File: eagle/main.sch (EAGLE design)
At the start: 16 parts, among them IC1 74HC164D, IC2 74LS139D, Q1 BSS84, Q2 BSS84, Q3 BSS84

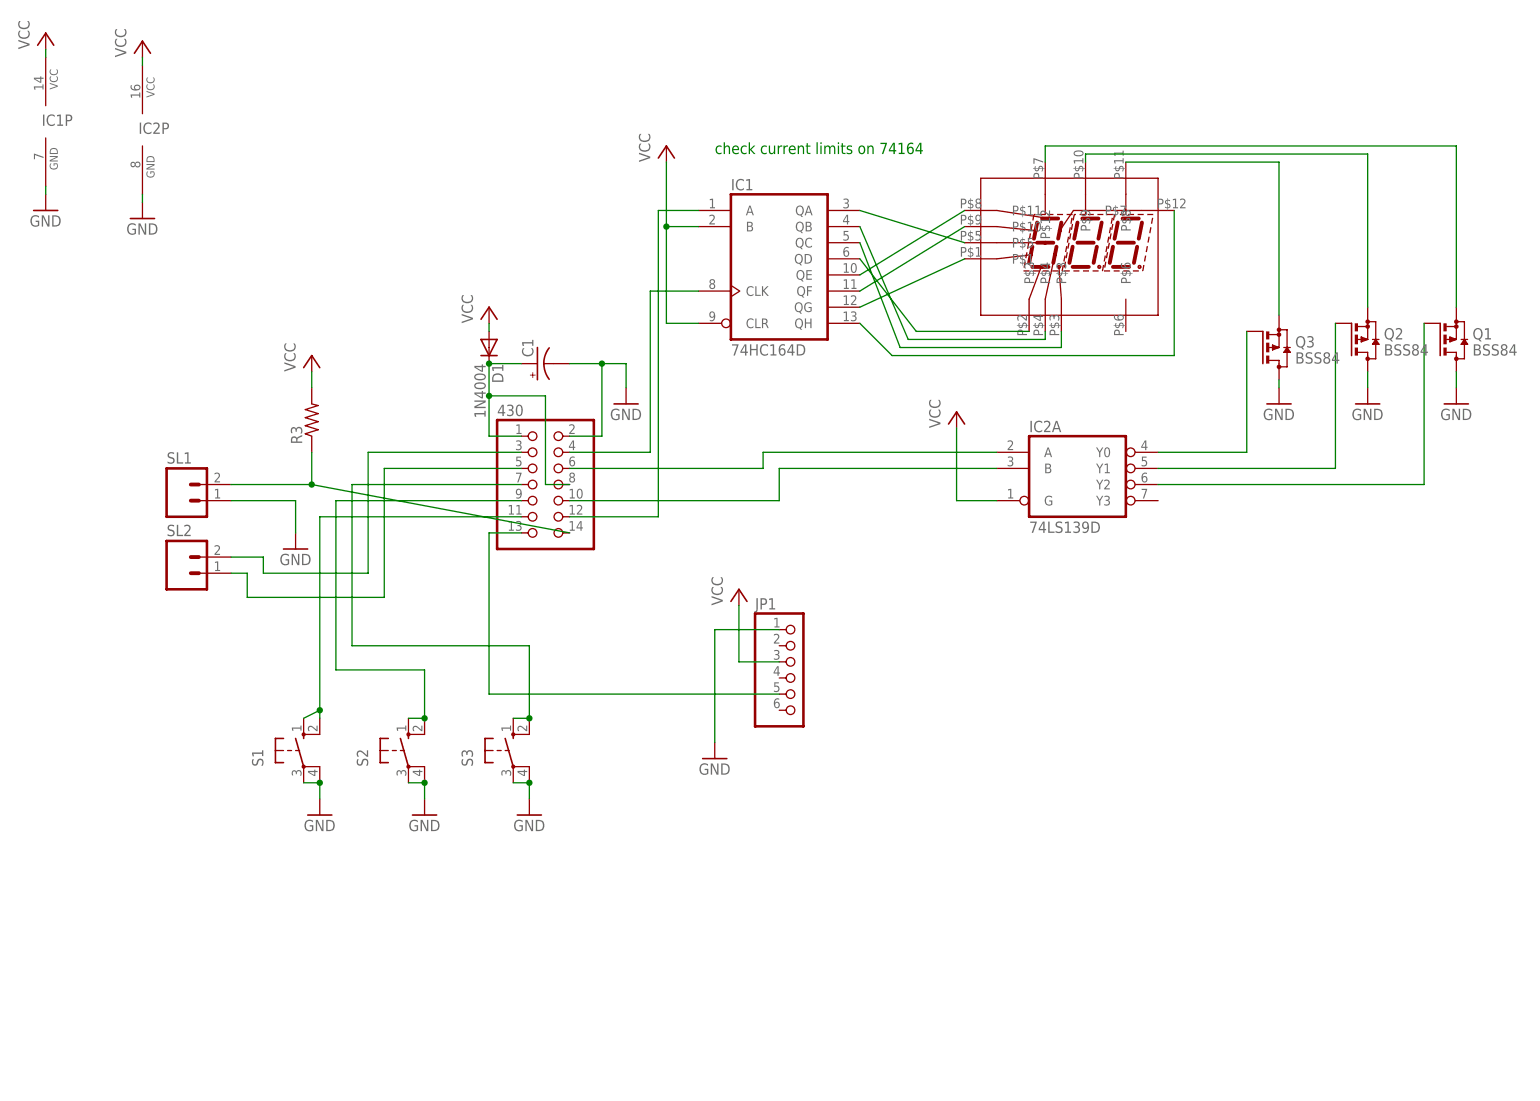
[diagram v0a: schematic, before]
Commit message: The 430 might not blow up after these edits
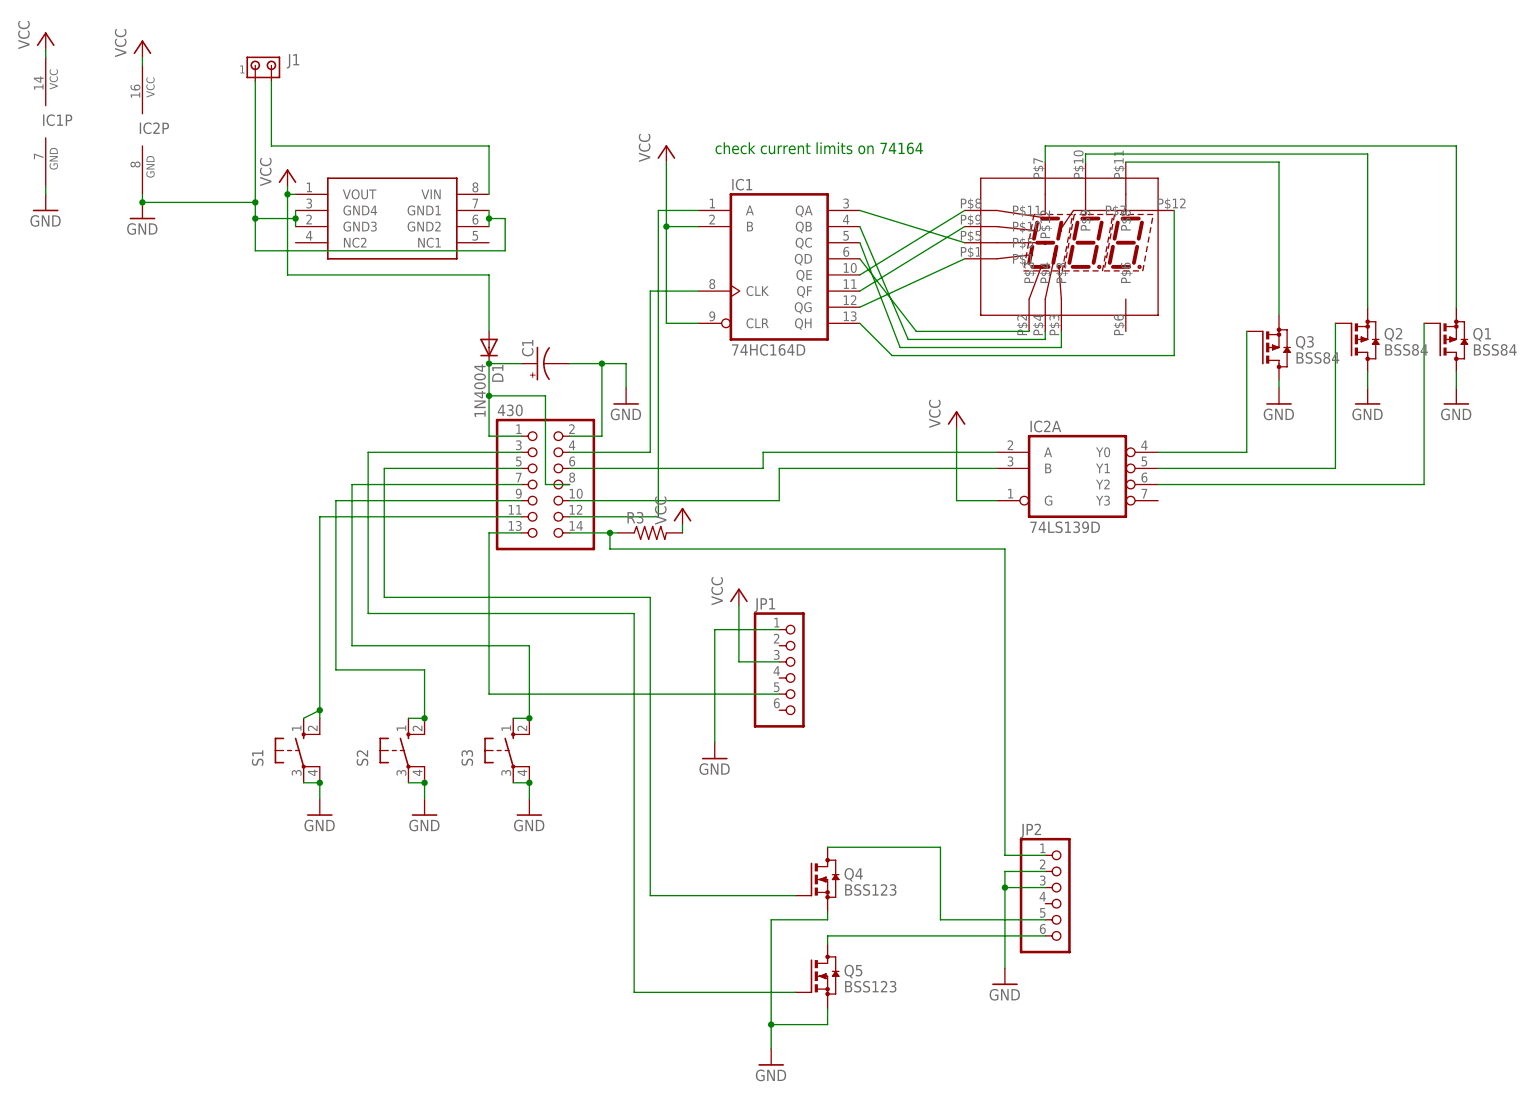
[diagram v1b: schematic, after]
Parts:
- removed SL1, SL2: (no value), con-amp-quick:M02
- added J1: (no value), con-amp:MTA02-100
- added JP2: (no value), pinhead:PINHD-1X6
- added Q4, Q5: BSS123, transistor-small-signal:BSS123
- added U$2: L78L33ABD, mjg:L78L33ABD
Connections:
- new net N$23: JP2.5, Q4.D
- new net N$28: JP2.6, Q5.D
- new net N$30: J1.2, U$2.VIN
- net GND: now also J1.1, JP2.2, JP2.3, Q4.S, Q5.S, U$2.GND1, U$2.GND2, U$2.GND3, U$2.GND4; no longer SL1.1
- net N$17: now also JP2.1; no longer SL1.2
- net N$19: now also Q5.G; no longer SL2.2
- net N$20: now also Q4.G; no longer SL2.1
- net VCC: now also U$2.VOUT
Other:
- moved on the sheet: R3

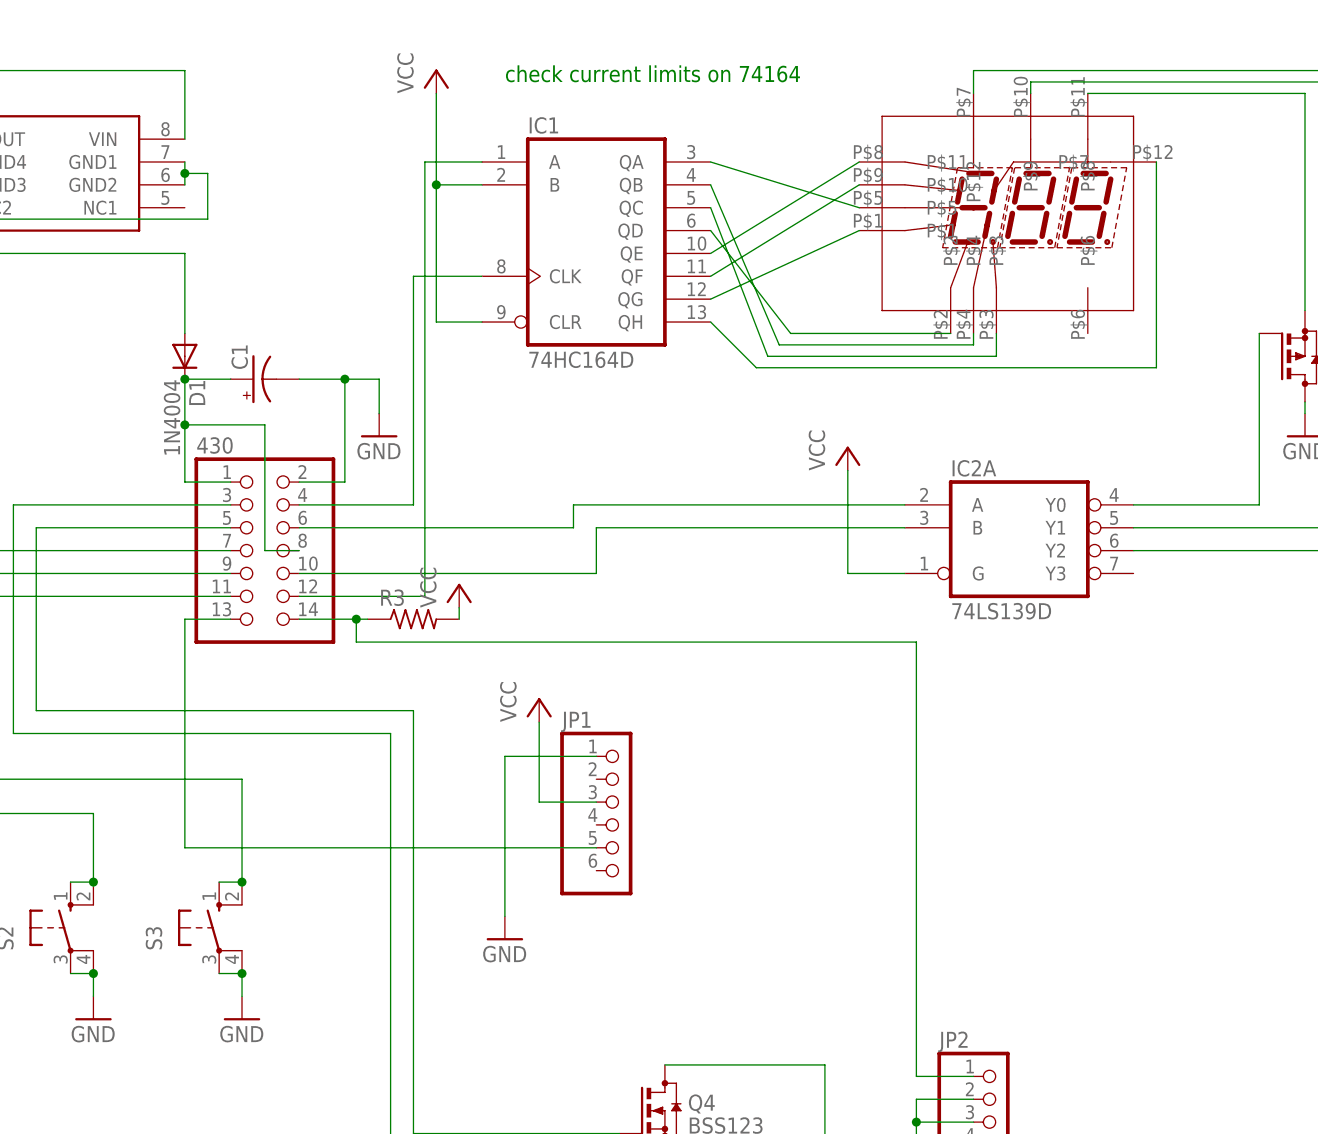
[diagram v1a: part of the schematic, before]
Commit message: updated values and added example parts order for Newark
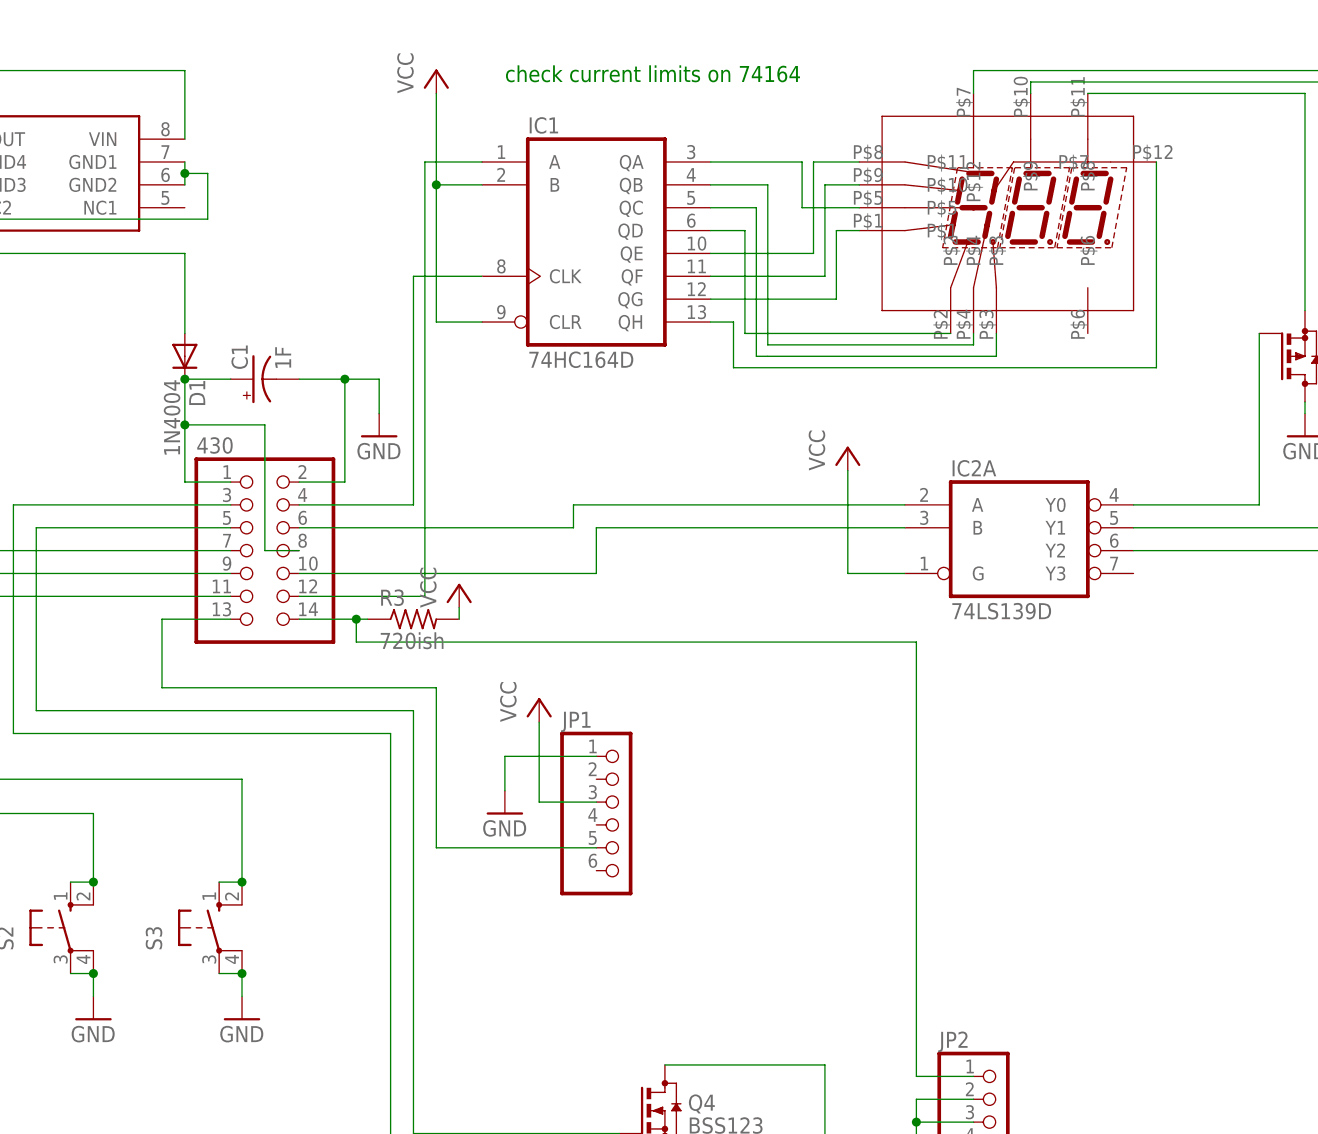
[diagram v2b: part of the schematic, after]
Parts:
- C1: value (none) -> 1F
- R3: value (none) -> 720ish
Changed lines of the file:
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@@
 <part name="P+1" library="supply1" deviceset="VCC" device=""/>
 <part name="GND1" library="supply1" deviceset="GND" device=""/>
-<part name="C1" library="rcl" deviceset="CPOL-US" device="E5-13"/>
+<part name="C1" library="rcl" deviceset="CPOL-US" device="E5-13" value="1F"/>
 <part name="D1" library="diode" deviceset="1N4004" device=""/>
-<part name="R3" library="rcl" deviceset="R-US_" device="R0805"/>
+<part name="R3" library="rcl" deviceset="R-US_" device="R0805" value="720ish"/>
 <part name="GND2" library="supply1" deviceset="GND" device=""/>
 <part name="P+3" library="supply1" deviceset="VCC" device=""/>
@@
 <instance part="IC2" gate="A" x="158.75" y="53.34"/>
 <instance part="P+5" gate="VCC" x="105.41" y="34.29"/>
-<instance part="GND7" gate="1" x="101.6" y="7.62"/>
+<instance part="GND7" gate="1" x="101.6" y="21.59"/>
 <instance part="P+6" gate="VCC" x="139.7" y="62.23"/>
 <instance part="IC1" gate="P" x="-3.81" y="107.95"/>
@@
 <segment>
 <pinref part="U$1" gate="G$1" pin="P$2"/>
-<wire x1="133.35" y1="74.93" x2="151.13" y2="74.93" width="0.1524" layer="91"/>
+<wire x1="128.27" y1="74.93" x2="151.13" y2="74.93" width="0.1524" layer="91"/>
 <pinref part="IC1" gate="A" pin="QD"/>
-<wire x1="124.46" y1="86.36" x2="133.35" y2="74.93" width="0.1524" layer="91"/>
+<wire x1="124.46" y1="86.36" x2="128.27" y2="86.36" width="0.1524" layer="91"/>
+<wire x1="128.27" y1="86.36" x2="128.27" y2="74.93" width="0.1524" layer="91"/>
 </segment>
 </net>
 <net name="N$6" class="0">
 <segment>
-<wire x1="132.08" y1="73.66" x2="153.67" y2="73.66" width="0.1524" layer="91"/>
+<wire x1="130.81" y1="73.66" x2="153.67" y2="73.66" width="0.1524" layer="91"/>
 <pinref part="U$1" gate="G$1" pin="P$4"/>
 <wire x1="153.67" y1="73.66" x2="153.67" y2="74.93" width="0.1524" layer="91"/>
 <pinref part="IC1" gate="A" pin="QB"/>
-<wire x1="124.46" y1="91.44" x2="132.08" y2="73.66" width="0.1524" layer="91"/>
+<wire x1="124.46" y1="91.44" x2="130.81" y2="91.44" width="0.1524" layer="91"/>
+<wire x1="130.81" y1="91.44" x2="130.81" y2="73.66" width="0.1524" layer="91"/>
 </segment>
 </net>
@@
 <wire x1="156.21" y1="72.39" x2="156.21" y2="74.93" width="0.1524" layer="91"/>
 <pinref part="IC1" gate="A" pin="QC"/>
-<wire x1="124.46" y1="88.9" x2="130.81" y2="72.39" width="0.1524" layer="91"/>
+<wire x1="124.46" y1="88.9" x2="129.54" y2="88.9" width="0.1524" layer="91"/>
+<wire x1="129.54" y1="88.9" x2="129.54" y2="72.39" width="0.1524" layer="91"/>
+<wire x1="129.54" y1="72.39" x2="130.81" y2="72.39" width="0.1524" layer="91"/>
 </segment>
 </net>
@@
 <segment>
 <pinref part="IC1" gate="A" pin="QH"/>
-<wire x1="124.46" y1="76.2" x2="129.54" y2="71.12" width="0.1524" layer="91"/>
-<wire x1="129.54" y1="71.12" x2="173.99" y2="71.12" width="0.1524" layer="91"/>
+<wire x1="124.46" y1="76.2" x2="127" y2="76.2" width="0.1524" layer="91"/>
+<wire x1="127" y1="76.2" x2="127" y2="71.12" width="0.1524" layer="91"/>
+<wire x1="127" y1="71.12" x2="173.99" y2="71.12" width="0.1524" layer="91"/>
 <pinref part="U$1" gate="G$1" pin="P$7"/>
 <wire x1="173.99" y1="71.12" x2="173.99" y2="93.98" width="0.1524" layer="91"/>
@@
 <pinref part="GND7" gate="1" pin="GND"/>
 <wire x1="111.76" y1="27.94" x2="101.6" y2="27.94" width="0.1524" layer="91"/>
-<wire x1="101.6" y1="27.94" x2="101.6" y2="10.16" width="0.1524" layer="91"/>
+<wire x1="101.6" y1="27.94" x2="101.6" y2="24.13" width="0.1524" layer="91"/>
 </segment>
 <segment>
@@
 <segment>
 <pinref part="430" gate="A" pin="13"/>
-<wire x1="71.12" y1="43.18" x2="66.04" y2="43.18" width="0.1524" layer="91"/>
-<wire x1="66.04" y1="43.18" x2="66.04" y2="17.78" width="0.1524" layer="91"/>
+<wire x1="71.12" y1="43.18" x2="63.5" y2="43.18" width="0.1524" layer="91"/>
+<wire x1="63.5" y1="43.18" x2="63.5" y2="35.56" width="0.1524" layer="91"/>
+<wire x1="63.5" y1="35.56" x2="93.98" y2="35.56" width="0.1524" layer="91"/>
 <pinref part="JP1" gate="A" pin="5"/>
-<wire x1="66.04" y1="17.78" x2="111.76" y2="17.78" width="0.1524" layer="91"/>
+<wire x1="93.98" y1="35.56" x2="93.98" y2="17.78" width="0.1524" layer="91"/>
+<wire x1="93.98" y1="17.78" x2="111.76" y2="17.78" width="0.1524" layer="91"/>
 </segment>
 </net>
@@
 <pinref part="IC1" gate="A" pin="QF"/>
 <pinref part="U$1" gate="G$1" pin="P$10"/>
-<wire x1="124.46" y1="81.28" x2="140.97" y2="91.44" width="0.1524" layer="91"/>
+<wire x1="124.46" y1="81.28" x2="137.16" y2="81.28" width="0.1524" layer="91"/>
+<wire x1="137.16" y1="81.28" x2="137.16" y2="91.44" width="0.1524" layer="91"/>
+<wire x1="137.16" y1="91.44" x2="140.97" y2="91.44" width="0.1524" layer="91"/>
 </segment>
 </net>
@@
 <pinref part="IC1" gate="A" pin="QE"/>
 <pinref part="U$1" gate="G$1" pin="P$11"/>
-<wire x1="124.46" y1="83.82" x2="140.97" y2="93.98" width="0.1524" layer="91"/>
+<wire x1="124.46" y1="83.82" x2="135.89" y2="83.82" width="0.1524" layer="91"/>
+<wire x1="135.89" y1="83.82" x2="135.89" y2="93.98" width="0.1524" layer="91"/>
+<wire x1="135.89" y1="93.98" x2="140.97" y2="93.98" width="0.1524" layer="91"/>
 </segment>
 </net>
@@
 <pinref part="U$1" gate="G$1" pin="P$1"/>
 <pinref part="IC1" gate="A" pin="QG"/>
-<wire x1="140.97" y1="86.36" x2="124.46" y2="78.74" width="0.1524" layer="91"/>
+<wire x1="140.97" y1="86.36" x2="138.43" y2="86.36" width="0.1524" layer="91"/>
+<wire x1="138.43" y1="86.36" x2="138.43" y2="78.74" width="0.1524" layer="91"/>
+<wire x1="138.43" y1="78.74" x2="124.46" y2="78.74" width="0.1524" layer="91"/>
 </segment>
 </net>
@@
 <pinref part="IC1" gate="A" pin="QA"/>
 <pinref part="U$1" gate="G$1" pin="P$5"/>
-<wire x1="124.46" y1="93.98" x2="140.97" y2="88.9" width="0.1524" layer="91"/>
-</segment>
-</net>
+<wire x1="124.46" y1="93.98" x2="134.62" y2="93.98" width="0.1524" layer="91"/>
+<wire x1="134.62" y1="93.98" x2="134.62" y2="88.9" width="0.1524" layer="91"/>
+<wire x1="134.62" y1="88.9" x2="140.97" y2="88.9" width="0.1524" layer="91"/>
+</segment>
+</net>

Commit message: Lots of hw changes and swapped parts.  Maybe your FTDI chip won't blow up with this one.
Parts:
- removed U$2: L78L33ABD, mjg:L78L33ABD
- added IC3: 317EMP, linear:317EMP
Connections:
- net GND: now also IC3.ADJ; no longer U$2.GND1, U$2.GND2, U$2.GND3, U$2.GND4
- net N$30: now also IC3.VI; no longer U$2.VIN
- net VCC: now also IC3.VO; no longer JP1.3, U$2.VOUT
